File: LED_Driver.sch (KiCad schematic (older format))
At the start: 6 parts, among them U2 AP5726

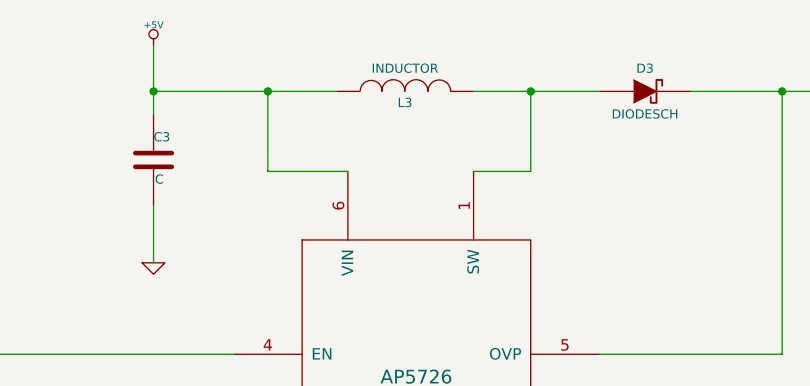
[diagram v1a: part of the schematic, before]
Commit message: 5.8 Associating and Placing the Power Protection and Filtering Module
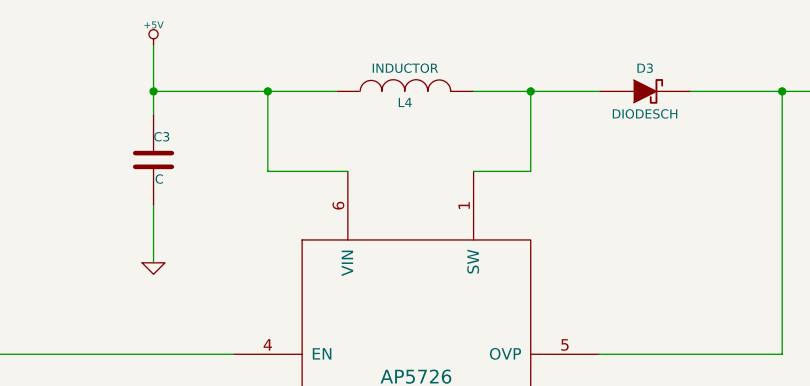
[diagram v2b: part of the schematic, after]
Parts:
- renumbered L3 to L4
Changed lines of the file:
@@
 $Descr A4 11693 8268
 encoding utf-8
-Sheet 5 9
+Sheet 4 9
 Title ""
 Date "23 feb 2014"
@@
 	2300 2400 3450 2400
 $Comp
-L GND #PWR18
+L GND #PWR21
 U 1 1 52F721EF
 P 4250 3950
-F 0 "#PWR18" H 4250 3950 30  0001 C CNN
+F 0 "#PWR21" H 4250 3950 30  0001 C CNN
 F 1 "GND" H 4250 3880 30  0001 C CNN
 F 2 "" H 4250 3950 60  0000 C CNN
@@
 	4250 3350 4250 3950
 $Comp
-L +5V #PWR16
+L +5V #PWR19
 U 1 1 52F72EB7
 P 3100 1050
-F 0 "#PWR16" H 3100 1140 20  0001 C CNN
+F 0 "#PWR19" H 3100 1140 20  0001 C CNN
 F 1 "+5V" H 3100 1140 30  0000 C CNN
 F 2 "" H 3100 1050 60  0000 C CNN
@@
 $EndComp
 $Comp
-L GND #PWR17
+L GND #PWR20
 U 1 1 52F72EC4
 P 3100 2000
-F 0 "#PWR17" H 3100 2000 30  0001 C CNN
+F 0 "#PWR20" H 3100 2000 30  0001 C CNN
 F 1 "GND" H 3100 1930 30  0001 C CNN
 F 2 "" H 3100 2000 60  0000 C CNN
@@
 $EndComp
 $Comp
-L INDUCTOR L3
+L INDUCTOR L4
 U 1 1 52F72F01
 P 4200 1250
-F 0 "L3" V 4150 1250 40  0000 C CNN
+F 0 "L4" V 4150 1250 40  0000 C CNN
 F 1 "INDUCTOR" V 4300 1250 40  0000 C CNN
 F 2 "~" H 4200 1250 60  0000 C CNN
@@
 Connection ~ 5850 1250
 $Comp
-L GND #PWR19
+L GND #PWR22
 U 1 1 52F72FE8
 P 8450 2250
-F 0 "#PWR19" H 8450 2250 30  0001 C CNN
+F 0 "#PWR22" H 8450 2250 30  0001 C CNN
 F 1 "GND" H 8450 2180 30  0001 C CNN
 F 2 "" H 8450 2250 60  0000 C CNN

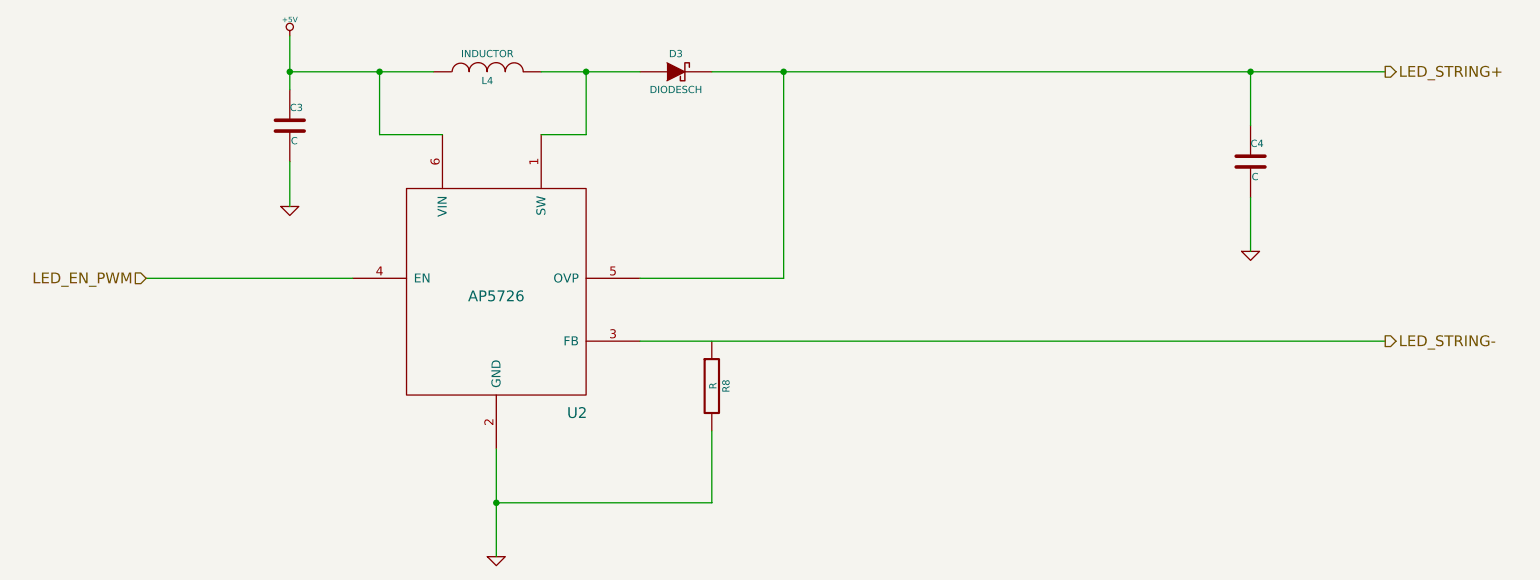
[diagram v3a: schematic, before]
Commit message: 5.11 Video 1/2 Associating and Placing the LED Driver Module
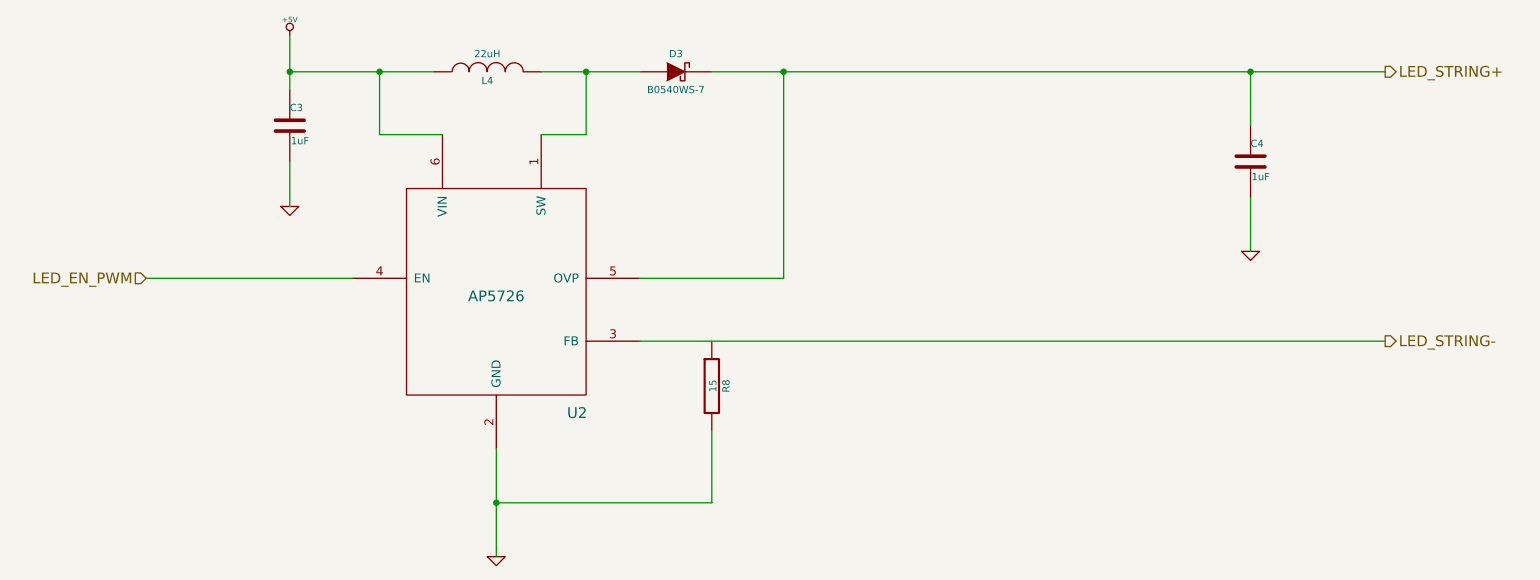
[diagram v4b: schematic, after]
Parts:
- C3, C4: value C -> 1uF
- D3: value DIODESCH -> B0540WS-7; MFG Part Number (none) -> B0540WS-7
- L4: value INDUCTOR -> 22uH; MFG Part Number (none) -> NR4012T220M
- R8: value R -> 15
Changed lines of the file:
@@
 P 3100 1550
 F 0 "C3" H 3100 1650 40  0000 L CNN
-F 1 "C" H 3106 1465 40  0000 L CNN
+F 1 "1uF" H 3106 1465 40  0000 L CNN
 F 2 "~" H 3138 1400 30  0000 C CNN
 F 3 "~" H 3100 1550 60  0000 C CNN
@@
 P 8450 1750
 F 0 "C4" H 8450 1850 40  0000 L CNN
-F 1 "C" H 8456 1665 40  0000 L CNN
+F 1 "1uF" H 8456 1665 40  0000 L CNN
 F 2 "~" H 8488 1600 30  0000 C CNN
 F 3 "~" H 8450 1750 60  0000 C CNN
@@
 P 4200 1250
 F 0 "L4" V 4150 1250 40  0000 C CNN
-F 1 "INDUCTOR" V 4300 1250 40  0000 C CNN
+F 1 "22uH" V 4300 1250 40  0000 C CNN
 F 2 "~" H 4200 1250 60  0000 C CNN
 F 3 "~" H 4200 1250 60  0000 C CNN
+F 4 "NR4012T220M" H 4200 1250 60  0001 C CNN "MFG Part Number"
 	1    4200 1250
 	0    -1   -1   0
@@
 P 5250 1250
 F 0 "D3" H 5250 1350 40  0000 C CNN
-F 1 "DIODESCH" H 5250 1150 40  0000 C CNN
+F 1 "B0540WS-7" H 5250 1150 40  0000 C CNN
 F 2 "~" H 5250 1250 60  0000 C CNN
 F 3 "~" H 5250 1250 60  0000 C CNN
+F 4 "B0540WS-7" H 5250 1250 60  0001 C CNN "MFG Part Number"
 	1    5250 1250
 	1    0    0    -1
@@
 P 5450 3000
 F 0 "R8" V 5530 3000 40  0000 C CNN
-F 1 "R" V 5457 3001 40  0000 C CNN
+F 1 "15" V 5457 3001 40  0000 C CNN
 F 2 "~" V 5380 3000 30  0000 C CNN
 F 3 "~" H 5450 3000 30  0000 C CNN

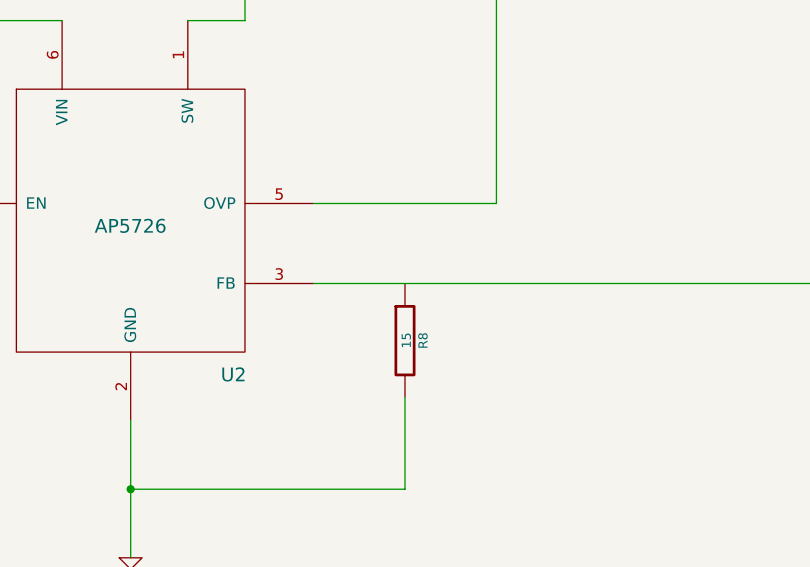
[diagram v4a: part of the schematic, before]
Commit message: Cleanup/ERC checks, etc (on my own, no video)
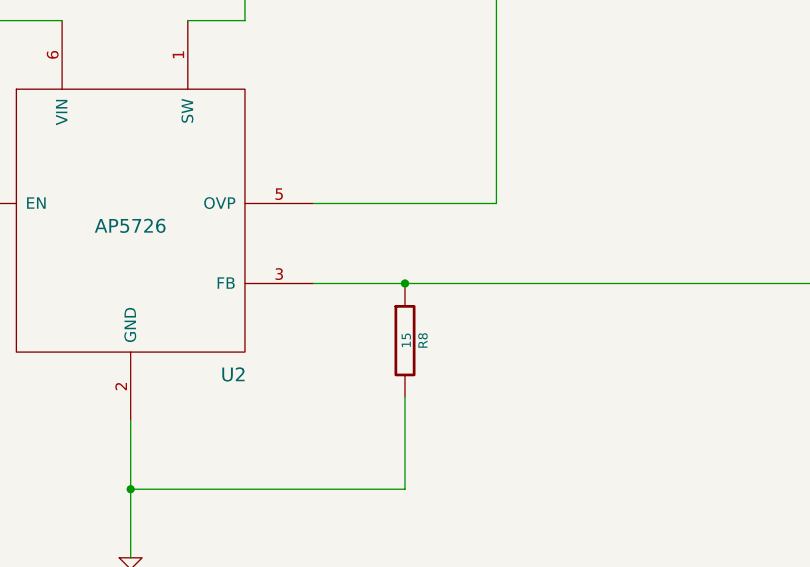
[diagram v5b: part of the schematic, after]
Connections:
- net LED_STRING-: now also R8.1
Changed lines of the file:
@@
 Wire Wire Line
 	8450 1950 8450 2250
+Connection ~ 5450 2750
 $EndSCHEMATC
